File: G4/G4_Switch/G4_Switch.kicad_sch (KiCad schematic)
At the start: 30 parts, among them J1 Conn_01x09_Socket, J2 Conn_01x09_Socket, J3 DB25_Plug, U1 NUCLEO-G491RE, U2 74HC594, U3 74HC594, U4 ULN2003A, U5 ULN2003A

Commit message: updated G4_Switch
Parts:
- added J_GNDA1: Conn_01x01_Female, Connector_PinHeader_2.54mm:PinHeader_1x01_P2.54mm_Vertical, symbol Connector:Conn_01x01_Female
- C1, C2: footprint (none) -> Capacitor_THT:C_Disc_D3.4mm_W2.1mm_P2.50mm
- U1: footprint G4Lib:MODULE_NUCLEO-G491RE20 -> G4Lib:MODULE_NUCLEO-G491RE20noar
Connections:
- net GNDA: now also J_GNDA1.1 (Pin_1)
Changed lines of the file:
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@@
+    (stroke (width 0) (type default))
+  )
+  (wire (pts (xy 245.11 34.29) (xy 245.745 34.29))
     (stroke (width 0) (type default))
   )
@@
       (effects (font (size 1.27 1.27)))
     )
-    (property "Footprint" "" (at 120.65 193.3448 0)
+    (property "Footprint" "Capacitor_THT:C_Disc_D3.4mm_W2.1mm_P2.50mm" (at 120.65 193.3448 0)
       (effects (font (size 1.27 1.27)) hide)
     )
@@
       (effects (font (size 1.27 1.27)))
     )
-    (property "Footprint" "G4Lib:MODULE_NUCLEO-G491RE20" (at 181.61 67.31 90)
+    (property "Footprint" "G4Lib:MODULE_NUCLEO-G491RE20noar" (at 181.61 67.31 90)
       (effects (font (size 1.27 1.27)) (justify bottom) hide)
     )
@@
       (effects (font (size 1.27 1.27)))
     )
-    (property "Footprint" "G4Lib:MODULE_NUCLEO-G491RE20" (at 101.6 67.31 90)
+    (property "Footprint" "G4Lib:MODULE_NUCLEO-G491RE20noar" (at 101.6 67.31 90)
       (effects (font (size 1.27 1.27)) (justify bottom) hide)
     )
@@
     )
   )
+  (symbol (lib_id "power:GNDA") (at 245.11 34.29 270) (unit 1)
+    (in_bom yes) (on_board yes) (dnp no) (fields_autoplaced)
+    (property "Reference" "#PWR010" (at 238.76 34.29 0)
+      (effects (font (size 1.27 1.27)) hide)
+    )
+    (property "Value" "GNDA" (at 241.3 34.29 90)
+      (effects (font (size 1.27 1.27)) (justify right))
+    )
+    (property "Footprint" "" (at 245.11 34.29 0)
+      (effects (font (size 1.27 1.27)) hide)
+    )
+    (property "Datasheet" "" (at 245.11 34.29 0)
+      (effects (font (size 1.27 1.27)) hide)
+    )
+    (pin "1")
+    (instances
+      (project "G4_Switch"
+        (path "/2f876161-0d68-4cd5-b08d-6033cbf09a5a"
+          (reference "#PWR010") (unit 1)
+        )
+      )
+    )
+  )
   (symbol (lib_id "Connector:Conn_01x09_Socket") (at 267.97 97.79 0) (unit 1)
     (in_bom yes) (on_board yes) (dnp no) (fields_autoplaced)
@@
       (effects (font (size 1.27 1.27)))
     )
-    (property "Footprint" "" (at 82.55 160.3248 0)
+    (property "Footprint" "Capacitor_THT:C_Disc_D3.4mm_W2.1mm_P2.50mm" (at 82.55 160.3248 0)
       (effects (font (size 1.27 1.27)) hide)
     )
@@
         (path "/2f876161-0d68-4cd5-b08d-6033cbf09a5a"
           (reference "#PWR0105") (unit 1)
+        )
+      )
+    )
+  )
+  (symbol (lib_id "Connector:Conn_01x01_Female") (at 250.825 34.29 0) (unit 1)
+    (in_bom yes) (on_board yes) (dnp no) (fields_autoplaced)
+    (property "Reference" "J_GNDA1" (at 252.73 33.02 0)
+      (effects (font (size 1.27 1.27)) (justify left))
+    )
+    (property "Value" "Conn_01x01_Female" (at 252.73 35.56 0)
+      (effects (font (size 1.27 1.27)) (justify left))
+    )
+    (property "Footprint" "Connector_PinHeader_2.54mm:PinHeader_1x01_P2.54mm_Vertical" (at 250.825 34.29 0)
+      (effects (font (size 1.27 1.27)) hide)
+    )
+    (property "Datasheet" "~" (at 250.825 34.29 0)
+      (effects (font (size 1.27 1.27)) hide)
+    )
+    (pin "1")
+    (instances
+      (project "G4_Switch"
+        (path "/2f876161-0d68-4cd5-b08d-6033cbf09a5a"
+          (reference "J_GNDA1") (unit 1)
         )
       )
@@
       (effects (font (size 1.27 1.27)))
     )
-    (property "Footprint" "G4Lib:MODULE_NUCLEO-G491RE20" (at 44.45 87.63 90)
+    (property "Footprint" "G4Lib:MODULE_NUCLEO-G491RE20noar" (at 44.45 87.63 90)
       (effects (font (size 1.27 1.27)) (justify bottom) hide)
     )

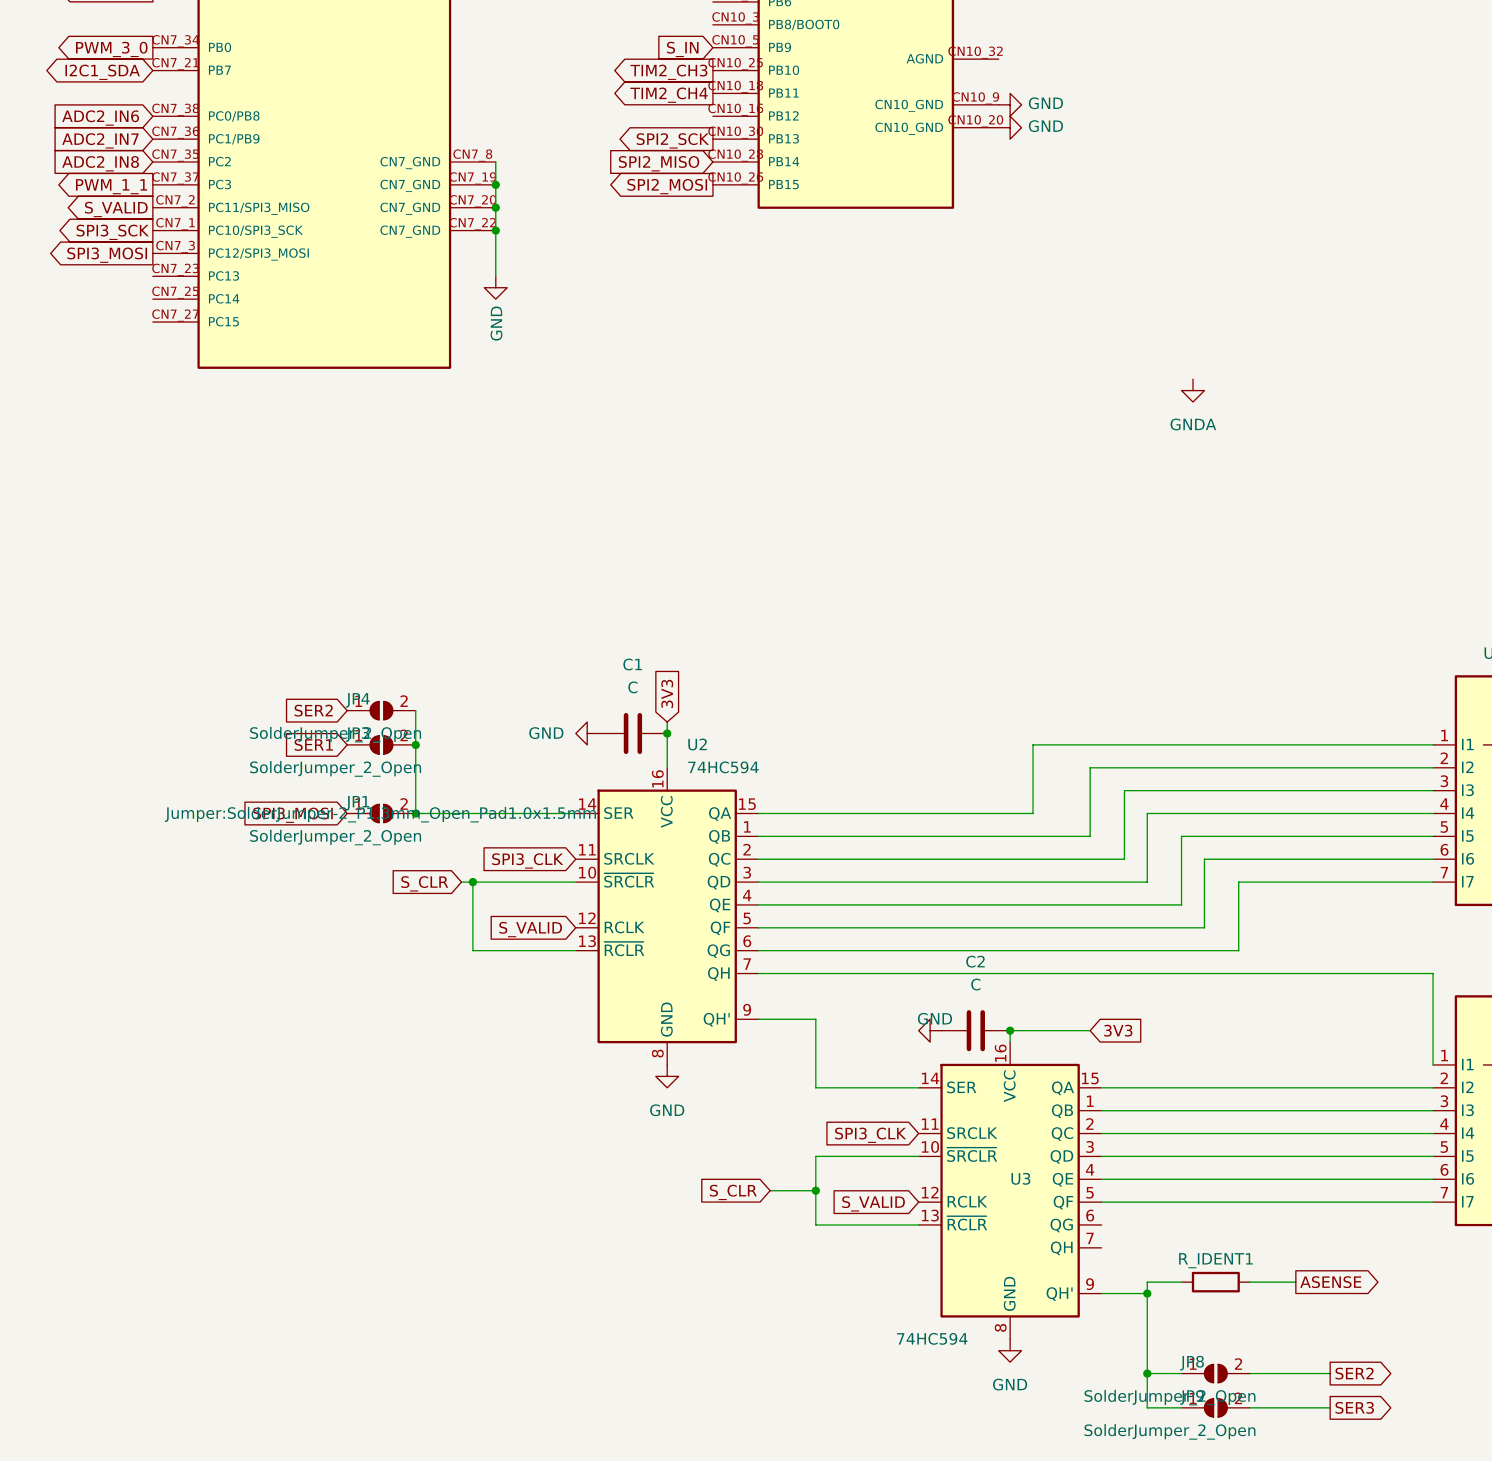
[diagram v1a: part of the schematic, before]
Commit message: updated G4_Switch, DRC run ok
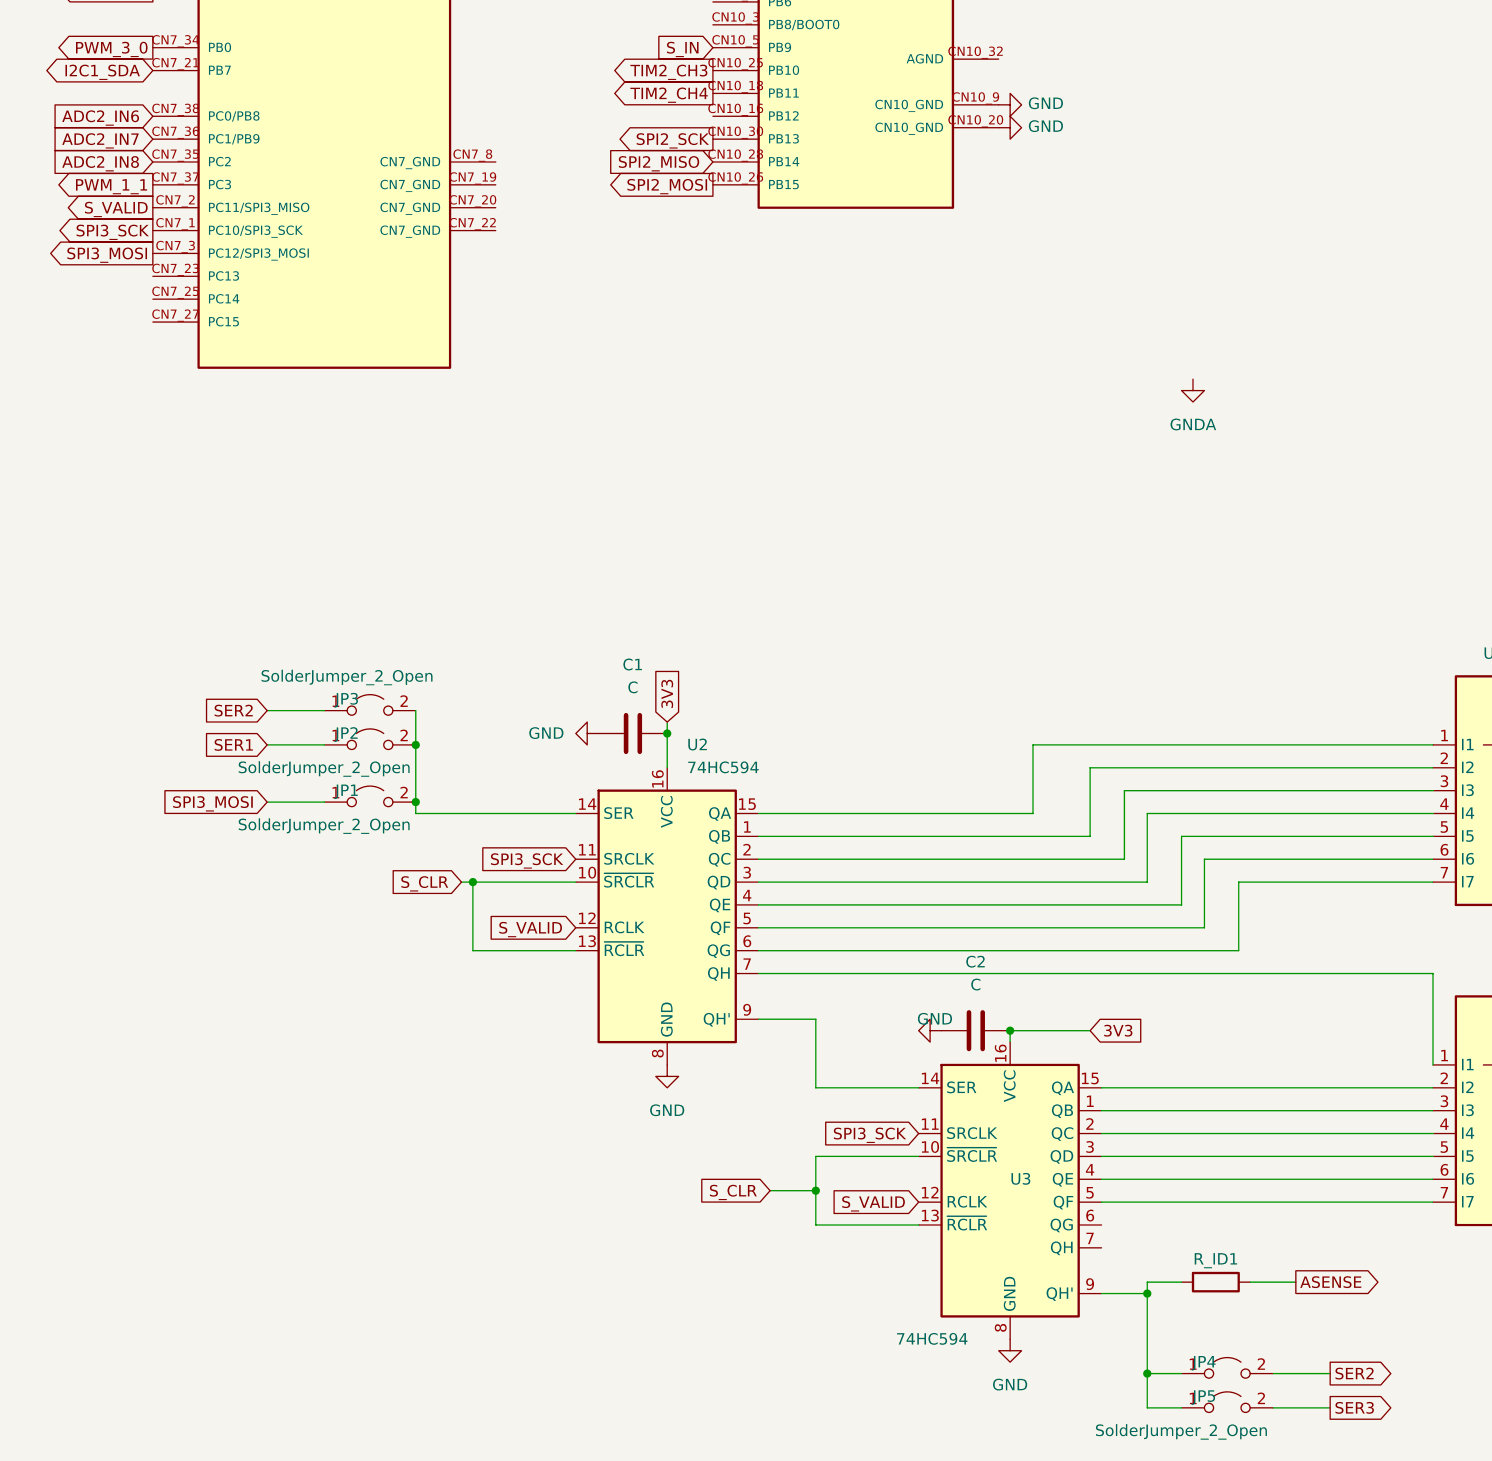
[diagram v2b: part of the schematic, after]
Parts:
- removed JP1, JP3, JP8, JP9: SolderJumper_2_Open, Jumper:SolderJumper-2_P1.3mm_Open_Pad1.0x1.5mm, symbol Jumper:SolderJumper_2_Open
- added JP1, JP2, JP4, JP5: SolderJumper_2_Open, Connector_PinHeader_2.54mm:PinHeader_1x02_P2.54mm_Vertical, symbol Jumper:Jumper_2_Open
- JP3: renamed from JP4; footprint Jumper:SolderJumper-2_P1.3mm_Open_Pad1.0x1.5mm -> Connector_PinHeader_2.54mm:PinHeader_1x02_P2.54mm_Vertical; symbol Jumper:SolderJumper_2_Open -> Jumper:Jumper_2_Open
- renumbered R_IDENT1 to R_ID1
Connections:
- net SPI3_CLK is gone; now on net SPI3_SCK: U2.11 (SRCLK), U3.11 (SRCLK)
- net GND: no longer U1.CN7_19 (CN7_GND), U1.CN7_20 (CN7_GND), U1.CN7_22 (CN7_GND), U1.CN7_8 (CN7_GND)
- net SER1: now also JP2.1 (A)
- net SER2: now also JP4.2 (B)
- net SER3: now also JP5.2 (B)
- net SPI3_MOSI: now also JP1.1 (A)
- net at R_ID1.2, U3.9 (QH'): now also JP4.1 (A), JP5.1 (A)
- net at JP3.2 (B), U2.14 (SER): now also JP1.2 (B), JP2.2 (B)
